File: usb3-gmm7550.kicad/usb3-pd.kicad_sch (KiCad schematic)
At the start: 0 parts

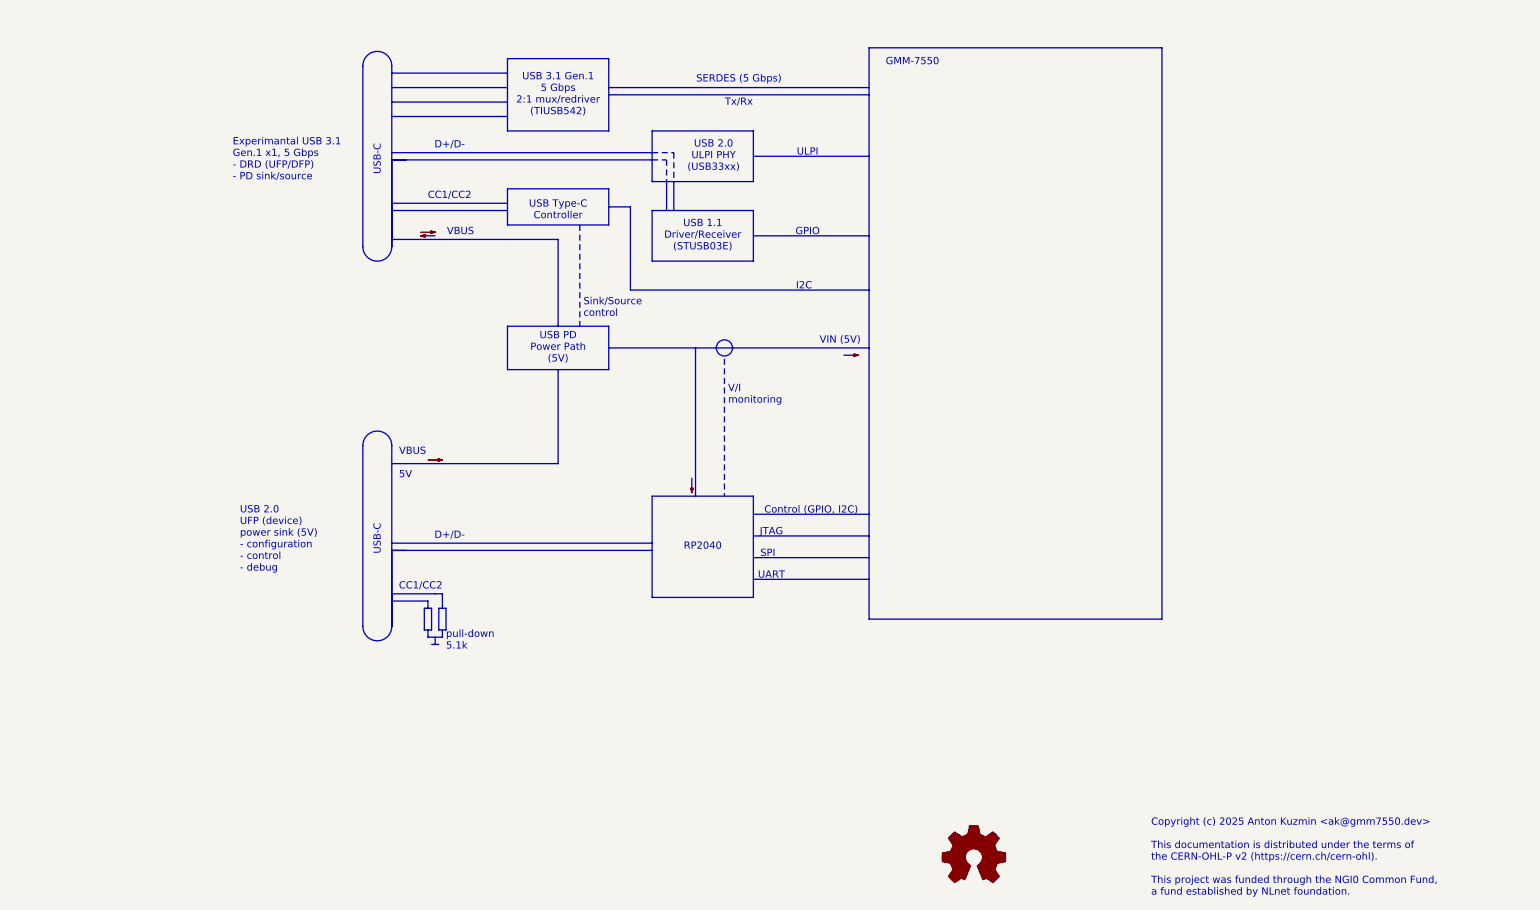
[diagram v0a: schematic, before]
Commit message: USB 3 adapter schematic -- WIP: USB 3 and Power Delivery pages
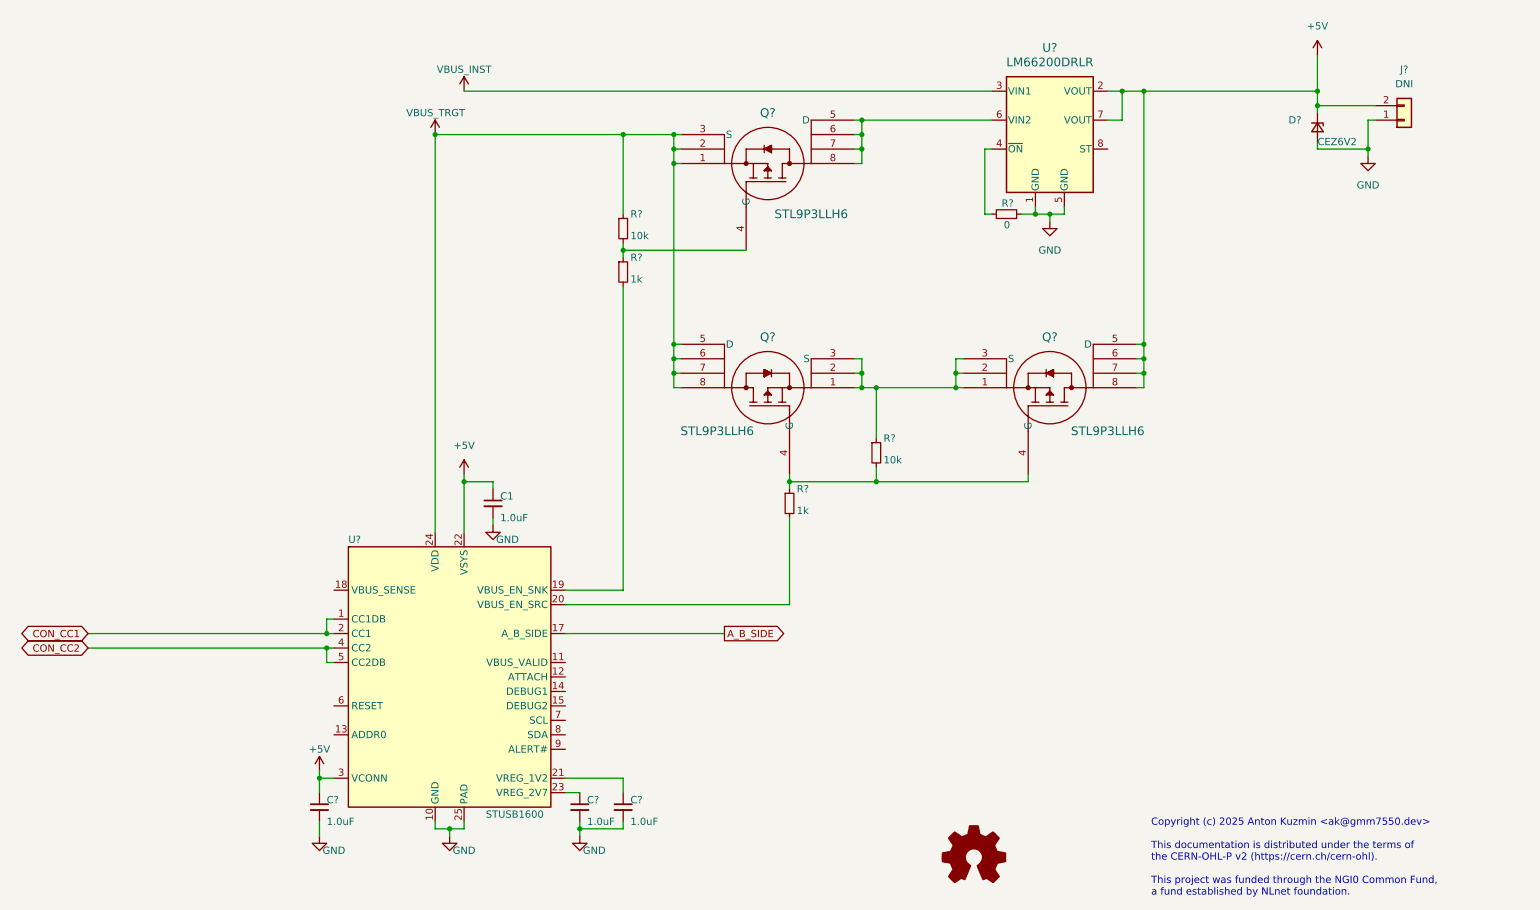
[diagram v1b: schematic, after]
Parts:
- added C1, C? (x3): 1.0uF, Capacitor_SMD:C_0402_1005Metric, symbol Device:C_Small
- added D?: CEZ6V2, Diode_SMD:D_SOD-523, symbol Device:D_Zener_Small
- added J?: DNI, Connector_Molex:Molex_Micro-Fit_3.0_43045-0200_2x01_P3.00mm_Horizontal, symbol Connector_Generic:Conn_01x02
- added Q? (x3): STL9P3LLH6, POWERFLAT_3P3X3P3_STM, symbol usb3-gmm7550:STL9P3LLH6
- added R? (x2): 1k, Resistor_SMD:R_0402_1005Metric, symbol Device:R_Small
- added R? (x2): 10k, Resistor_SMD:R_0402_1005Metric, symbol Device:R_Small
- added R?: 0, Resistor_SMD:R_0402_1005Metric, symbol Device:R_Small
- added U?: STUSB1600, Package_DFN_QFN:QFN-24-1EP_4x4mm_P0.5mm_EP2.7x2.7mm_ThermalVias, symbol usb3-gmm7550:STUSB1600
- added U?: LM66200DRLR, SOT-5X3_DRL_TEX, symbol usb3-gmm7550:LM66200DRLR
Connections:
- new net: Q?.4 (G), R?.1, R?.2
- new net: R?.2, U?.19 (VBUS_EN_SNK)
- new net: Q?.1, Q?.1, Q?.2, Q?.2, Q?.3 (S), Q?.3 (S), R?.1
- new net: Q?.4 (G), Q?.4 (G), R?.1, R?.2
- new net: R?.2, U?.20 (VBUS_EN_SRC)
- new net: C?.1, U?.21 (VREG_1V2)
- new net: C?.1, U?.23 (VREG_2V7)
- new net: Q?.5 (D), Q?.6, Q?.7, Q?.8, U?.6 (VIN2)
- new net: R?.1, U?.4 (~{ON})
- new net +5V: C1.1, C?.1, D?.1 (K), J?.2 (Pin_2), Q?.5 (D), Q?.6, Q?.7, Q?.8, U?.2 (VOUT), U?.22 (VSYS), U?.3 (VCONN), U?.7 (VOUT)
- new net A_B_SIDE: U?.17 (A_B_SIDE)
- new net CON_CC1: U?.1 (CC1DB), U?.2 (CC1)
- new net CON_CC2: U?.4 (CC2), U?.5 (CC2DB)
- new net GND: C1.2, C?.2, C?.2, C?.2, D?.2 (A), J?.1 (Pin_1), R?.2, U?.1 (GND), U?.10 (GND), U?.25 (PAD), U?.5 (GND)
- new net VBUS_INST: U?.3 (VIN1)
- new net VBUS_TRGT: Q?.1, Q?.2, Q?.3 (S), Q?.5 (D), Q?.6, Q?.7, Q?.8, R?.1, U?.24 (VDD)
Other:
- note removed: "CC1/CC2"
- note removed: "Control (GPIO, I2C)"
- note removed: "D+/D-"
- note removed: "Experimantal USB 3.1 Gen.1 x1, 5 Gbps - DRD (UFP/DFP) - PD sink/source"
- note removed: "GMM-7550"
- note removed: "GPIO"
- note removed: "I2C"
- note removed: "JTAG"
- note removed: "RP2040"
- note removed: "SERDES (5 Gbps) Tx/Rx"
- note removed: "SPI"
- note removed: "Sink/Source control"
- note removed: "UART"
- note removed: "ULPI"
- note removed: "USB 1.1 Driver/Receiver (STUSB03E)"
- note removed: "USB 2.0 UFP (device) power sink (5V) - configuration - control - debug"
- note removed: "USB 2.0 ULPI PHY (USB33xx)"
- note removed: "USB 3.1 Gen.1 5 Gbps 2:1 mux/redriver (TIUSB542)"
- note removed: "USB PD Power Path (5V)"
- note removed: "USB Type-C Controller"
- note removed: "USB-C"
- note removed: "V/I monitoring"
- note removed: "VBUS"
- note removed: "VBUS 5V"
- note removed: "VIN (5V)"
- note removed: "pull-down 5.1k"

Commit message: USB 3 adapter schematic -- WIP: USB 1.1 and 2.0 page, connections to the GMM-7550 IOs
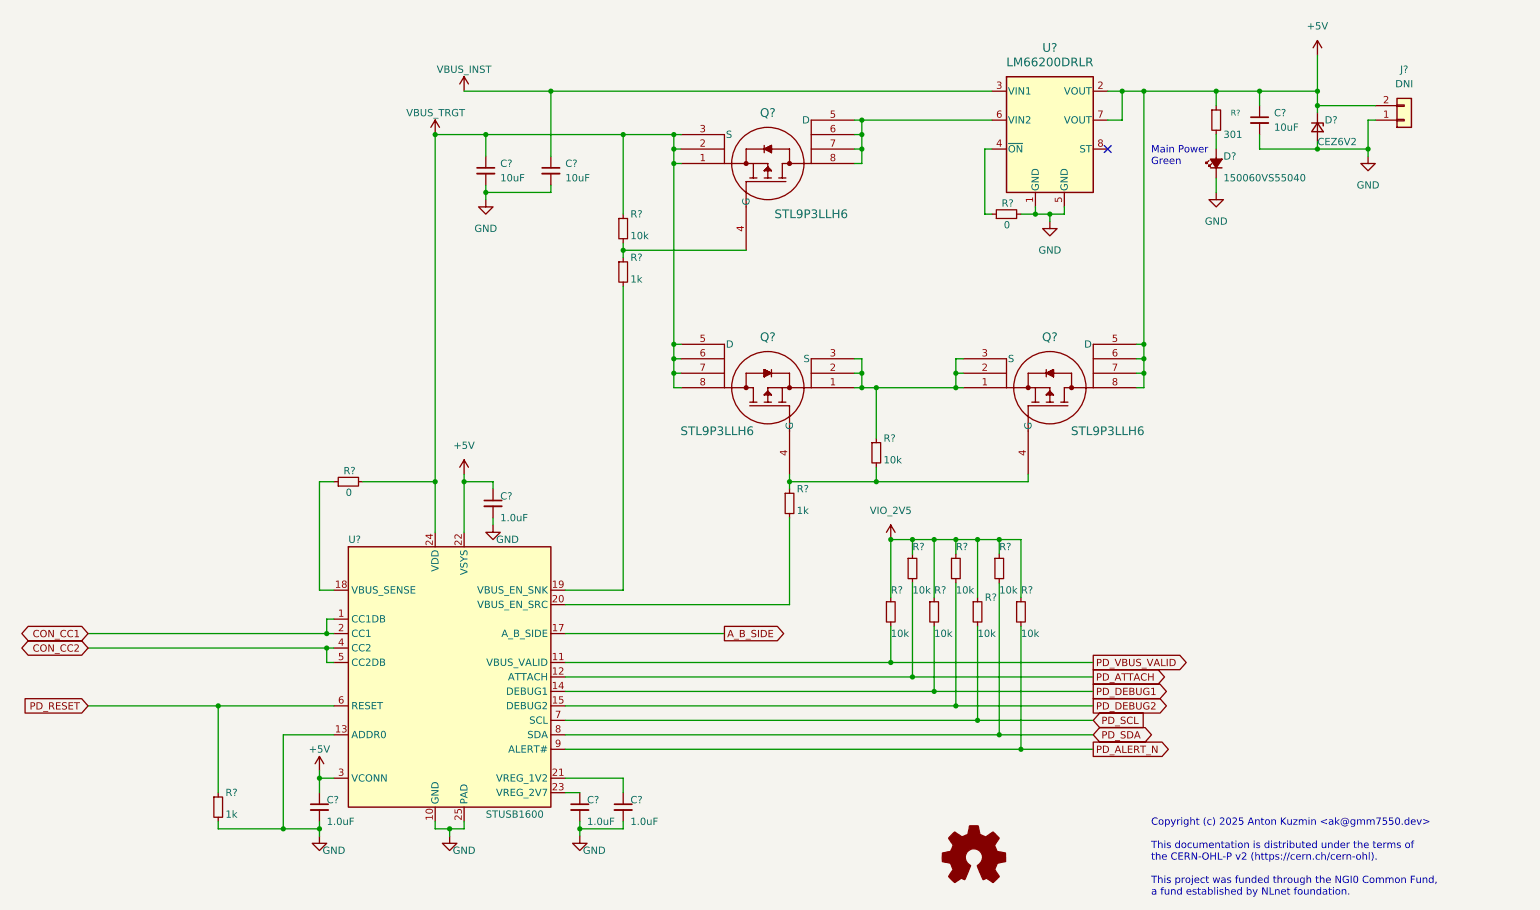
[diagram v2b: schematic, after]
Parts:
- added C? (x2): 10uF, Capacitor_SMD:C_0805_2012Metric, symbol Device:C_Small
- added D?: 150060VS55040, LED_SMD:LED_0603_1608Metric, symbol Device:LED_Small_Filled
- added R? (x7): 10k, Resistor_SMD:R_0402_1005Metric, symbol Device:R_Small
- added R?: 0, Resistor_SMD:R_0402_1005Metric, symbol Device:R_Small
- added R?: 1k, Resistor_SMD:R_0402_1005Metric, symbol Device:R_Small
- added R?: 301, Resistor_SMD:R_0402_1005Metric, symbol Device:R_Small
- renumbered C1 to C?
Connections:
- net +5V: now also C?.1, R?.1
- net GND: now also U?.13 (ADDR0), C?.2, C?.2, D?.1 (K), R?.2
- net VBUS_INST: now also C?.1
- net VBUS_TRGT: now also C?.1, R?.2
- net PD_VBUS_VALID: now reaches U?.11 (VBUS_VALID)
- net PD_VBUS_VALID: now also R?.2
- net PD_ATTACH: now reaches U?.12 (ATTACH)
- net PD_ATTACH: now also R?.2
- net PD_DEBUG1: now reaches U?.14 (DEBUG1)
- net PD_DEBUG1: now also R?.2
- net PD_DEBUG2: now reaches U?.15 (DEBUG2)
- net PD_DEBUG2: now also R?.2
- net at U?.18 (VBUS_SENSE): now also R?.1
- net PD_RESET: now reaches U?.6 (RESET)
- net PD_RESET: now also R?.1
- net PD_SCL: now reaches U?.7 (SCL)
- net PD_SCL: now also R?.2
- net PD_SDA: now reaches U?.8 (SDA)
- net PD_SDA: now also R?.2
- net PD_ALERT_N: now reaches U?.9 (ALERT#)
- net PD_ALERT_N: now also R?.2
- new net: D?.2 (A), R?.2
- new net VIO_2V5: R?.1, R?.1, R?.1, R?.1, R?.1, R?.1, R?.1
- no-connect marks 0 -> 1
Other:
- note added: "Main Power Green"

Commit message: USB 3 adapter schematic: revision 0.9 (pre-layout) is ready
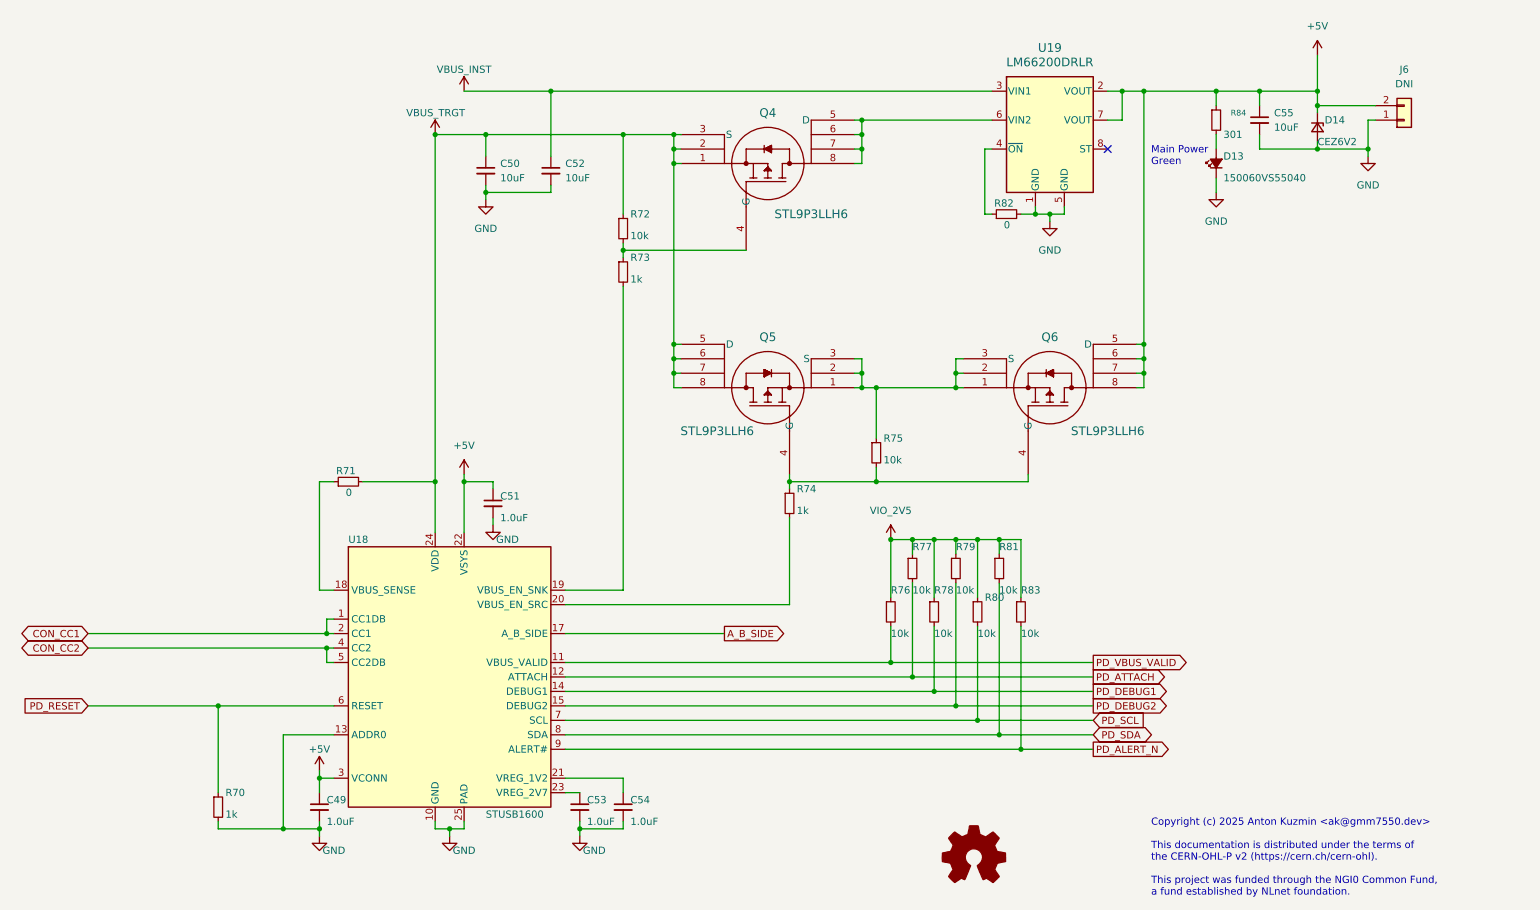
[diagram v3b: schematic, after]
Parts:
- added C50: 10uF, Capacitor_SMD:C_0805_2012Metric, symbol Device:C_Small
- gave numbers to parts that had none: 29
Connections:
- net GND: now also C50.2
- net VBUS_TRGT: now also C50.1; no longer C55.1
